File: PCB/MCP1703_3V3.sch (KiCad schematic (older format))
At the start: 3 parts, among them U9 MCP1703A-3302_SOT23

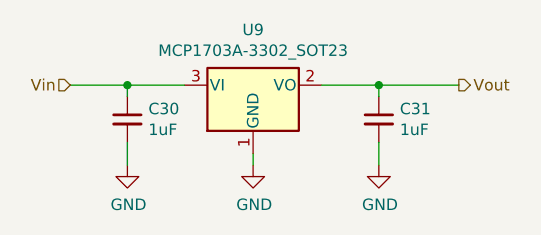
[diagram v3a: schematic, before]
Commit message: Added decoupling and voltage regulation
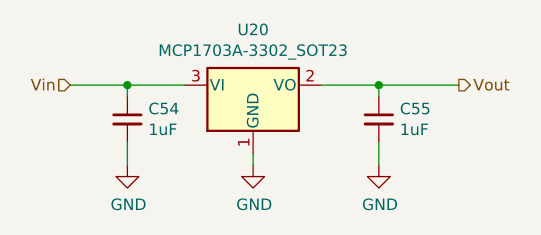
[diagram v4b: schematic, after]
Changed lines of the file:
@@
 $Descr A4 11693 8268
 encoding utf-8
-Sheet 12 27
+Sheet 12 28
 Title "ResQVenT"
 Date ""
@@
 AR Path="/5E880E11/5E942F93" Ref="U?"  Part="1"
 AR Path="/5E880E11/5E940C9C/5E942F93" Ref="U9"  Part="1"
-F 0 "U9" H 5900 4092 50  0000 C CNN
+AR Path="/5E97D98A/5EA9342A/5E942F93" Ref="U20"  Part="1"
+F 0 "U20" H 5900 4092 50  0000 C CNN
 F 1 "MCP1703A-3302_SOT23" H 5900 4001 50  0000 C CNN
 F 2 "Package_TO_SOT_SMD:SOT-23" H 5900 4050 50  0001 C CNN
@@
 U 1 1 5E944295
 P 5350 4000
-F 0 "C30" H 5442 4046 50  0000 L CNN
+AR Path="/5E880E11/5E940C9C/5E944295" Ref="C30"  Part="1"
+AR Path="/5E97D98A/5EA9342A/5E944295" Ref="C54"  Part="1"
+F 0 "C54" H 5442 4046 50  0000 L CNN
 F 1 "1uF" H 5442 3955 50  0000 L CNN
 F 2 "Capacitor_SMD:C_0603_1608Metric" H 5350 4000 50  0001 C CNN
@@
 U 1 1 5E944511
 P 6450 4000
-F 0 "C31" H 6542 4046 50  0000 L CNN
+AR Path="/5E880E11/5E940C9C/5E944511" Ref="C31"  Part="1"
+AR Path="/5E97D98A/5EA9342A/5E944511" Ref="C55"  Part="1"
+F 0 "C55" H 6542 4046 50  0000 L CNN
 F 1 "1uF" H 6542 3955 50  0000 L CNN
 F 2 "Capacitor_SMD:C_0603_1608Metric" H 6450 4000 50  0001 C CNN
@@
 U 1 1 5E944E6F
 P 5350 4200
-F 0 "#PWR087" H 5350 3950 50  0001 C CNN
+AR Path="/5E880E11/5E940C9C/5E944E6F" Ref="#PWR087"  Part="1"
+AR Path="/5E97D98A/5EA9342A/5E944E6F" Ref="#PWR0187"  Part="1"
+F 0 "#PWR0187" H 5350 3950 50  0001 C CNN
 F 1 "GND" H 5355 4027 50  0000 C CNN
 F 2 "" H 5350 4200 50  0001 C CNN
@@
 U 1 1 5E945281
 P 5900 4200
-F 0 "#PWR088" H 5900 3950 50  0001 C CNN
+AR Path="/5E880E11/5E940C9C/5E945281" Ref="#PWR088"  Part="1"
+AR Path="/5E97D98A/5EA9342A/5E945281" Ref="#PWR0188"  Part="1"
+F 0 "#PWR0188" H 5900 3950 50  0001 C CNN
 F 1 "GND" H 5905 4027 50  0000 C CNN
 F 2 "" H 5900 4200 50  0001 C CNN
@@
 U 1 1 5E9453D3
 P 6450 4200
-F 0 "#PWR089" H 6450 3950 50  0001 C CNN
+AR Path="/5E880E11/5E940C9C/5E9453D3" Ref="#PWR089"  Part="1"
+AR Path="/5E97D98A/5EA9342A/5E9453D3" Ref="#PWR0189"  Part="1"
+F 0 "#PWR0189" H 6450 3950 50  0001 C CNN
 F 1 "GND" H 6455 4027 50  0000 C CNN
 F 2 "" H 6450 4200 50  0001 C CNN
